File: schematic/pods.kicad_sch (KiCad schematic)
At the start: 0 parts

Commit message: Regen SKiDL artifacts with flat draft (date/tag churn only, BOM stable at 41)
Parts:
- added BST1: MT3608-5V-2A, Connector_PinHeader_2.54mm:PinHeader_1x04_P2.54mm_Vertical, symbol Connector_Generic:Conn_01x04
- added BT1: BLP673-4.2Ah, Connector_PinHeader_2.54mm:PinHeader_1x02_P2.54mm_Vertical, symbol Connector_Generic:Conn_01x02
- added C1, C10, C11, C3, C4, C6, C7, C8, C9: 100n-50V, Capacitor_SMD:C_0603_1608Metric, symbol Device:C
- added C2: 1000u-10V, Capacitor_THT:CP_Radial_D8.0mm_P3.50mm, symbol Device:C
- added C5: 10u-6V3, Capacitor_SMD:C_0603_1608Metric, symbol Device:C
- added CHG1: TP4056-TypeC-DW01A, Connector_PinHeader_2.54mm:PinHeader_1x04_P2.54mm_Vertical, symbol Connector_Generic:Conn_01x04
- added D1: 1N5819, Diode_THT:D_DO-41_SOD81_P7.62mm_Horizontal, symbol Diode:1N5819
- added D2: GROW-LED-5V-20CM-2A, Connector_PinHeader_2.54mm:PinHeader_1x02_P2.54mm_Vertical, symbol Connector_Generic:Conn_01x02
- added F1: Polyfuse-5A-hold, Fuse:Fuse_2920_7451Metric, symbol Device:Polyfuse
- added F2: Polyfuse-1.5A-hold, Fuse:Fuse_1812_4532Metric, symbol Device:Polyfuse
- added F3: Polyfuse-2.5A-hold, Fuse:Fuse_1812_4532Metric, symbol Device:Polyfuse
- added J1: WATER-1x03, Connector_PinHeader_2.54mm:PinHeader_1x03_P2.54mm_Vertical, symbol Connector_Generic:Conn_01x03
- added J2: SOIL-1x03, Connector_PinHeader_2.54mm:PinHeader_1x03_P2.54mm_Vertical, symbol Connector_Generic:Conn_01x03
- added J3: LIGHT-SENS-1x03, Connector_PinHeader_2.54mm:PinHeader_1x03_P2.54mm_Vertical, symbol Connector_Generic:Conn_01x03
- added J4: PROG-1x04, Connector_PinHeader_2.54mm:PinHeader_1x04_P2.54mm_Vertical, symbol Connector_Generic:Conn_01x04
- added M1: PUMP-5V-1A, Connector_PinHeader_2.54mm:PinHeader_1x02_P2.54mm_Vertical, symbol Connector_Generic:Conn_01x02
- added Q1, Q2: IRLZ44N, Package_TO_SOT_THT:TO-220-3_Vertical, symbol Transistor_FET:IRLZ44N
- added R1: 4.7K, Resistor_SMD:R_0603_1608Metric, symbol Device:R
- added R10, R11, R6: 1K, Resistor_SMD:R_0603_1608Metric, symbol Device:R
- added R2, R4: 220, Resistor_SMD:R_0603_1608Metric, symbol Device:R
- added R3, R5, R8, R9: 10K, Resistor_SMD:R_0603_1608Metric, symbol Device:R
- added R7: 330, Resistor_SMD:R_0603_1608Metric, symbol Device:R
- added SW1: BOOT-TACT, Button_Switch_THT:SW_PUSH-12mm, symbol Switch:SW_Push
- added U1A: ESP32-CAM-ODD, Connector_PinHeader_2.54mm:PinHeader_1x08_P2.54mm_Vertical, symbol Connector_Generic:Conn_01x08
- added U1B: ESP32-CAM-EVEN, Connector_PinHeader_2.54mm:PinHeader_1x08_P2.54mm_Vertical, symbol Connector_Generic:Conn_01x08
- added U2: DHT22, Connector_PinHeader_2.54mm:PinHeader_1x04_P2.54mm_Vertical, symbol Sensor:DHT11
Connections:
- new net: C6.1, R7.2
- new net: Q2.1 (G), R4.2, R5.1
- new net: R2.2, R3.1
- new net: J2.2 (Pin_2), R10.1
- new net: BT1.1 (Pin_1), CHG1.1 (Pin_1)
- new net: D2.2 (Pin_2), Q2.2 (D)
- new net: R8.2, SW1.1
- new net: R11.1, R9.1
- new net: J3.2 (Pin_2), R6.1
- new net +3V3: C4.1, C5.1, C7.1, C8.1, J2.1 (Pin_1), J3.1 (Pin_1), R1.1, R7.1, R8.1, U1A.6 (Pin_6), U2.1 (VDD)
- new net +5V: BST1.3 (Pin_3), C2.1, C3.1, F2.1, F3.1, J4.4 (Pin_4), U1A.1 (Pin_1), U1B.8 (Pin_8)
- new net BOOT_IO0: U1A.5 (Pin_5)
- new net BST_IN: BST1.1 (Pin_1), F1.2
- new net GND: BST1.2 (Pin_2), BST1.4 (Pin_4), BT1.2 (Pin_2), C1.2, C10.2, C2.2, C3.2, C4.2, C5.2, C6.2, C7.2, C8.2, C9.2, CHG1.2 (Pin_2), CHG1.4 (Pin_4), J1.3 (Pin_3), J2.3 (Pin_3), J3.3 (Pin_3), J4.3 (Pin_3), Q1.3 (S), Q2.3 (S), R1.2, R3.2, R5.2, R9.2, SW1.2, U1A.2 (Pin_2), U1A.7 (Pin_7), U1A.8 (Pin_8), U1B.6 (Pin_6), U2.2 (DATA), U2.4 (GND)
- new net GPIO12_NC: U1B.3 (Pin_3)
- new net LED_5V: D2.1 (Pin_1), F3.2
- new net LIGHT_AO: C1.1, R6.2, U1B.5 (Pin_5)
- new net LIGHT_GATE: R4.1, U1B.2 (Pin_2)
- new net PUMP_5V: C11.1, D1.1 (K), F2.2, M1.1 (Pin_1)
- new net PUMP_GATE: R2.1, U1B.1 (Pin_1)
- new net PUMP_GATE_Q: Q1.1 (G)
- new net PUMP_LO: C11.2, D1.2 (A), M1.2 (Pin_2), Q1.2 (D)
- new net SOIL_ADC: C9.1, R10.2, U1B.4 (Pin_4)
- new net SYS_PACK: CHG1.3 (Pin_3), F1.1
- new net TANK_VCC: J1.1 (Pin_1)
- new net U0RXD: J4.1 (Pin_1), U1A.3 (Pin_3)
- new net U0TXD: J4.2 (Pin_2), U1A.4 (Pin_4)
- new net WATER_ADC: C10.1, R11.2, U1B.7 (Pin_7)
- new net WATER_AO: J1.2 (Pin_2)
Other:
- removed sheet s_boost1
- removed sheet s_branches1
- removed sheet s_charge1
- removed sheet s_dht1
- removed sheet s_feed_fuse1
- removed sheet s_led1
- removed sheet s_lightsens1
- removed sheet s_mcu1
- removed sheet s_pump1
- removed sheet s_soil1
- removed sheet s_water1

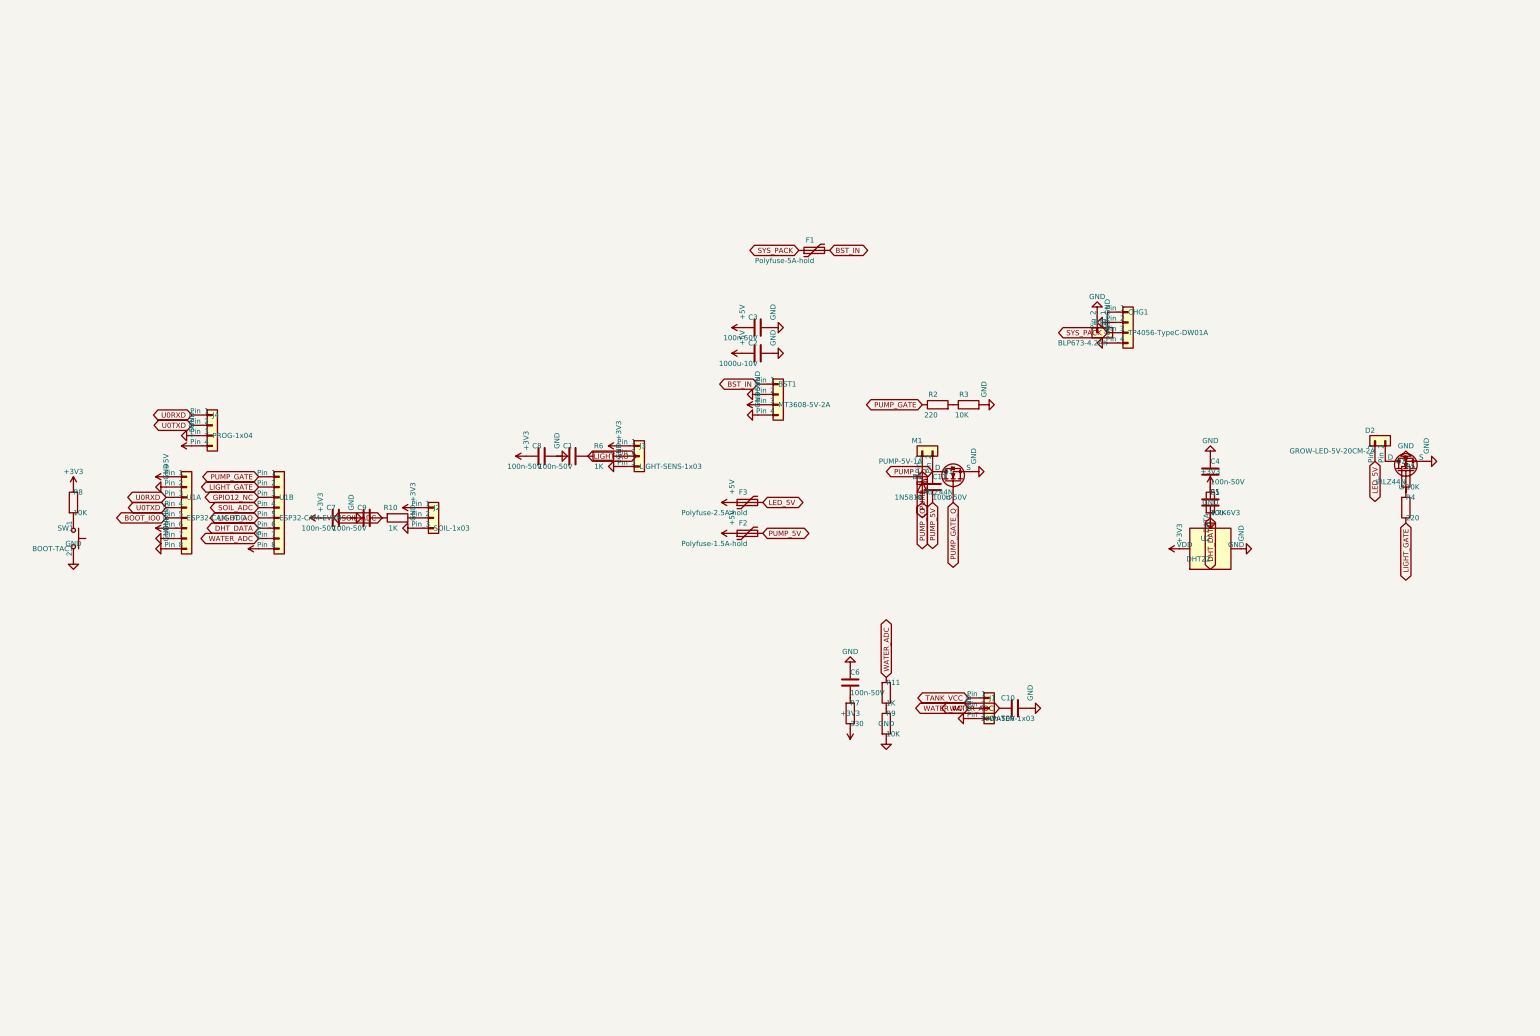
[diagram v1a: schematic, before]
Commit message: Audit fixes: doc footprint strings, GPIO33 LED note, D1 1N5822
04-wiring footprint column now matches pods.py/BOM (U2/SW1/M1/D2).
GPIO33 red-LED load disclosed like GPIO4. Pump flyback 1N5819 -> 1N5822
(DO-41, 3A class for 2A stall turn-off). ERC gate holds, full netlist
compare zero, PDF/final refreshed.
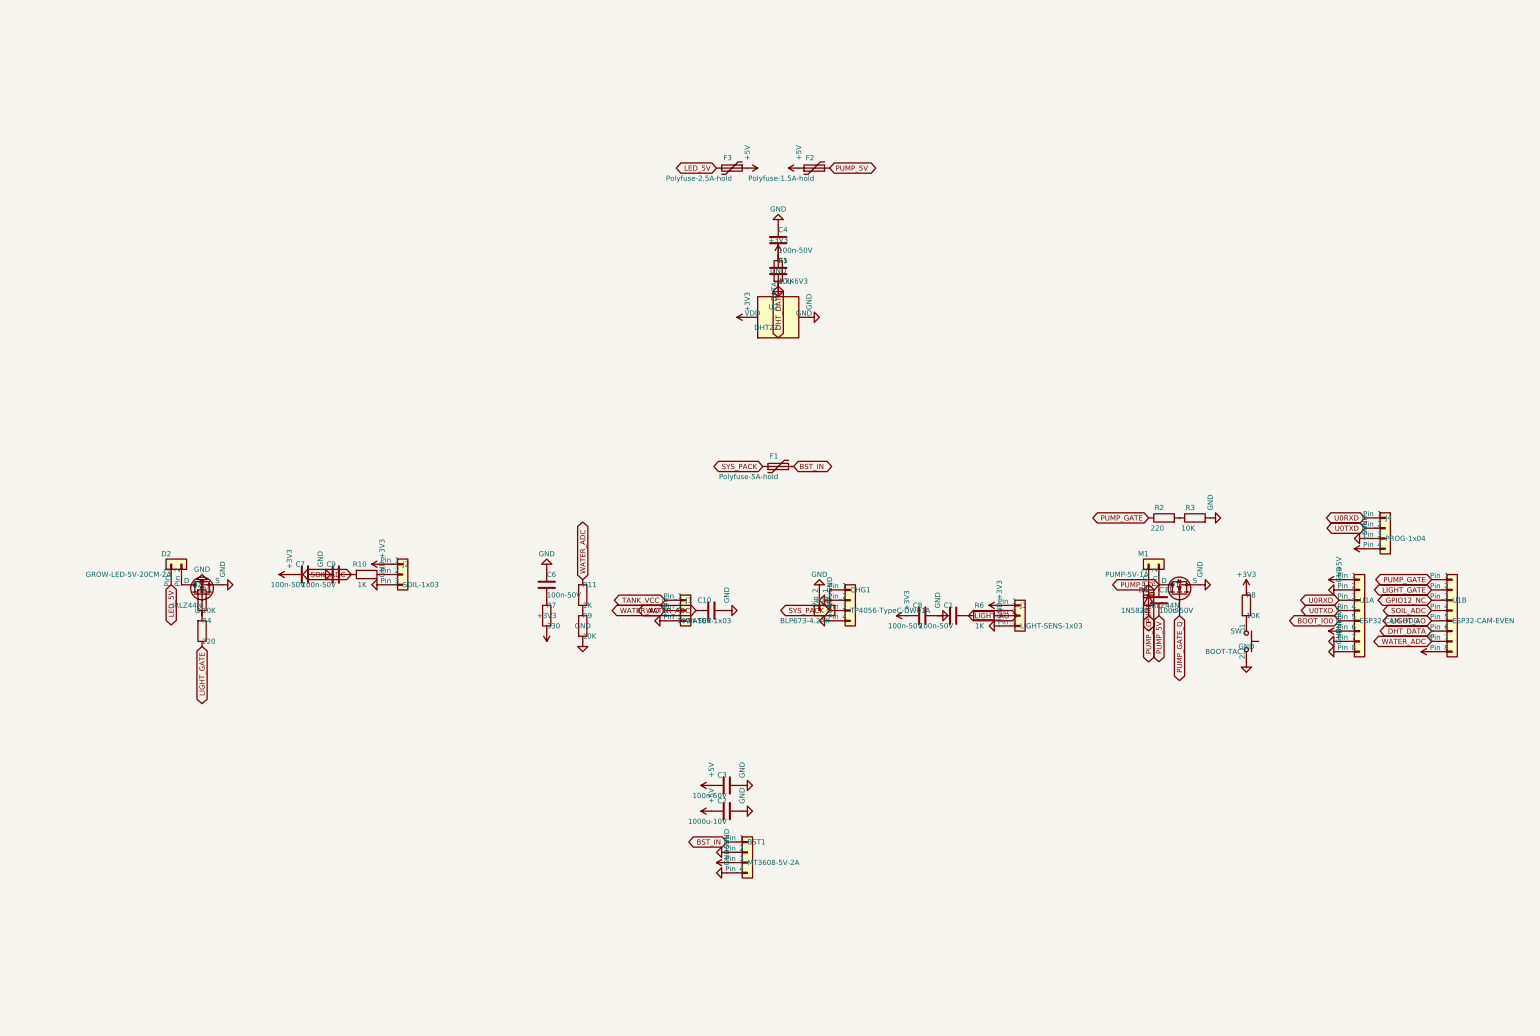
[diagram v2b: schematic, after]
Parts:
- D1: value 1N5819 -> 1N5822

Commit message: Owner decisions: OUT+/- rewire (CELL_NEG), XL6009 boost, server XOR
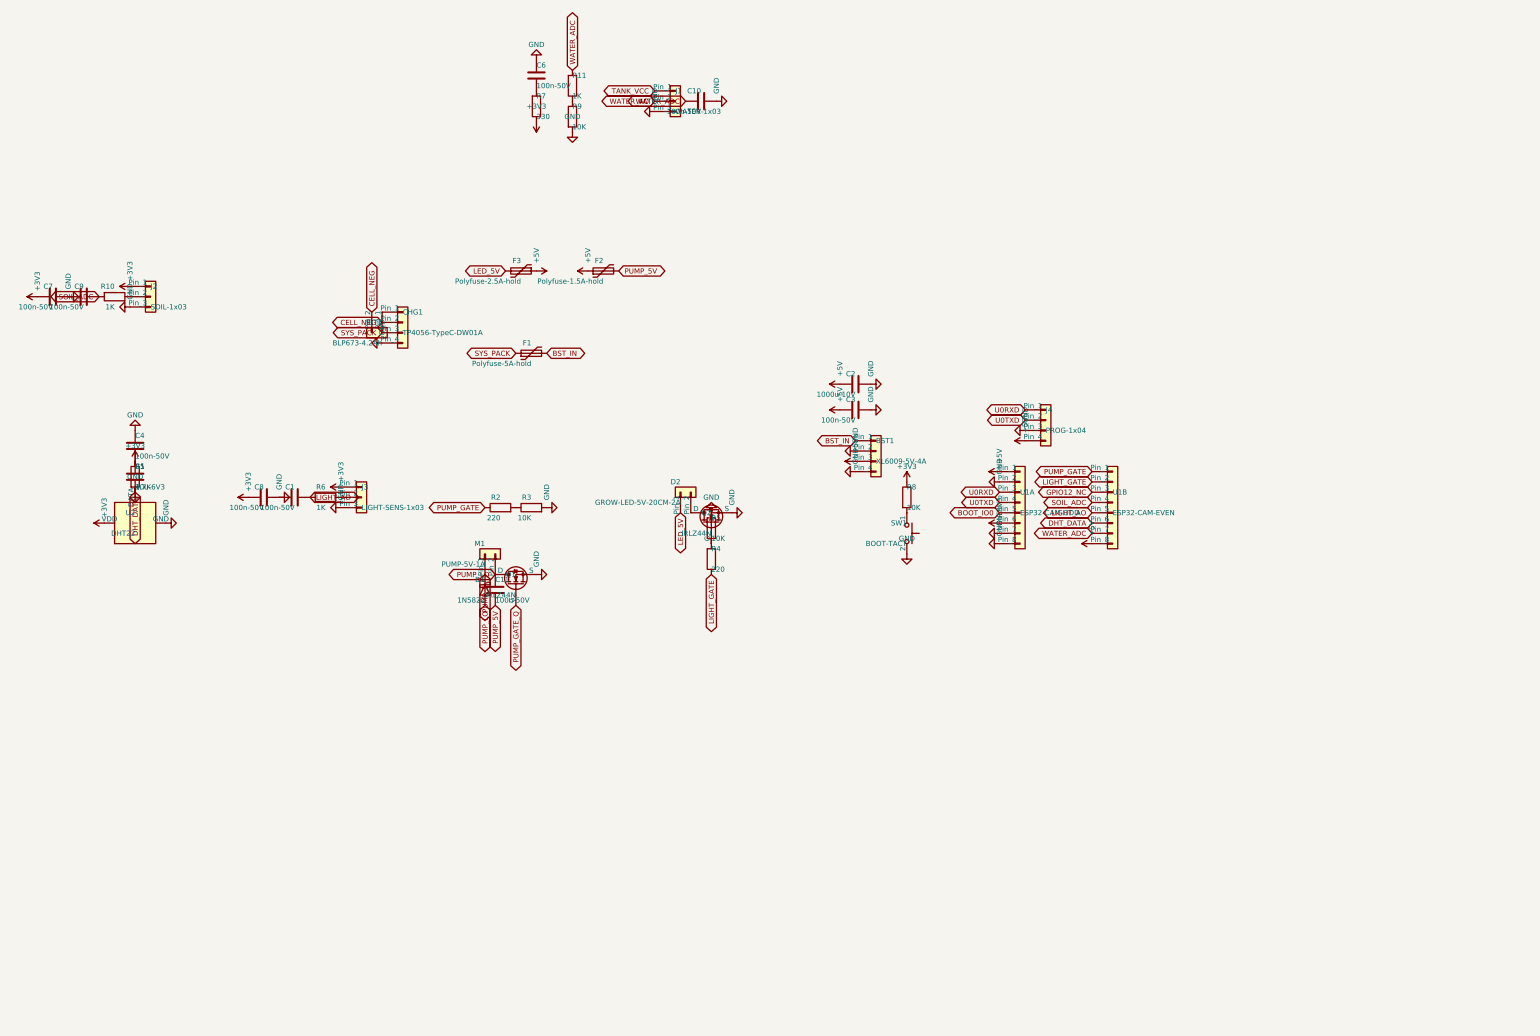
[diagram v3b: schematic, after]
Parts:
- BST1: value MT3608-5V-2A -> XL6009-5V-4A
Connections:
- net GND: no longer BT1.2 (Pin_2), CHG1.2 (Pin_2)
- new net CELL_NEG: BT1.2 (Pin_2), CHG1.2 (Pin_2)
